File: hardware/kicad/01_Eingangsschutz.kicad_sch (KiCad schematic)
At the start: 4 parts, among them K101 G6S-2F DC5 - C16707, Q111 DMN2056U-7

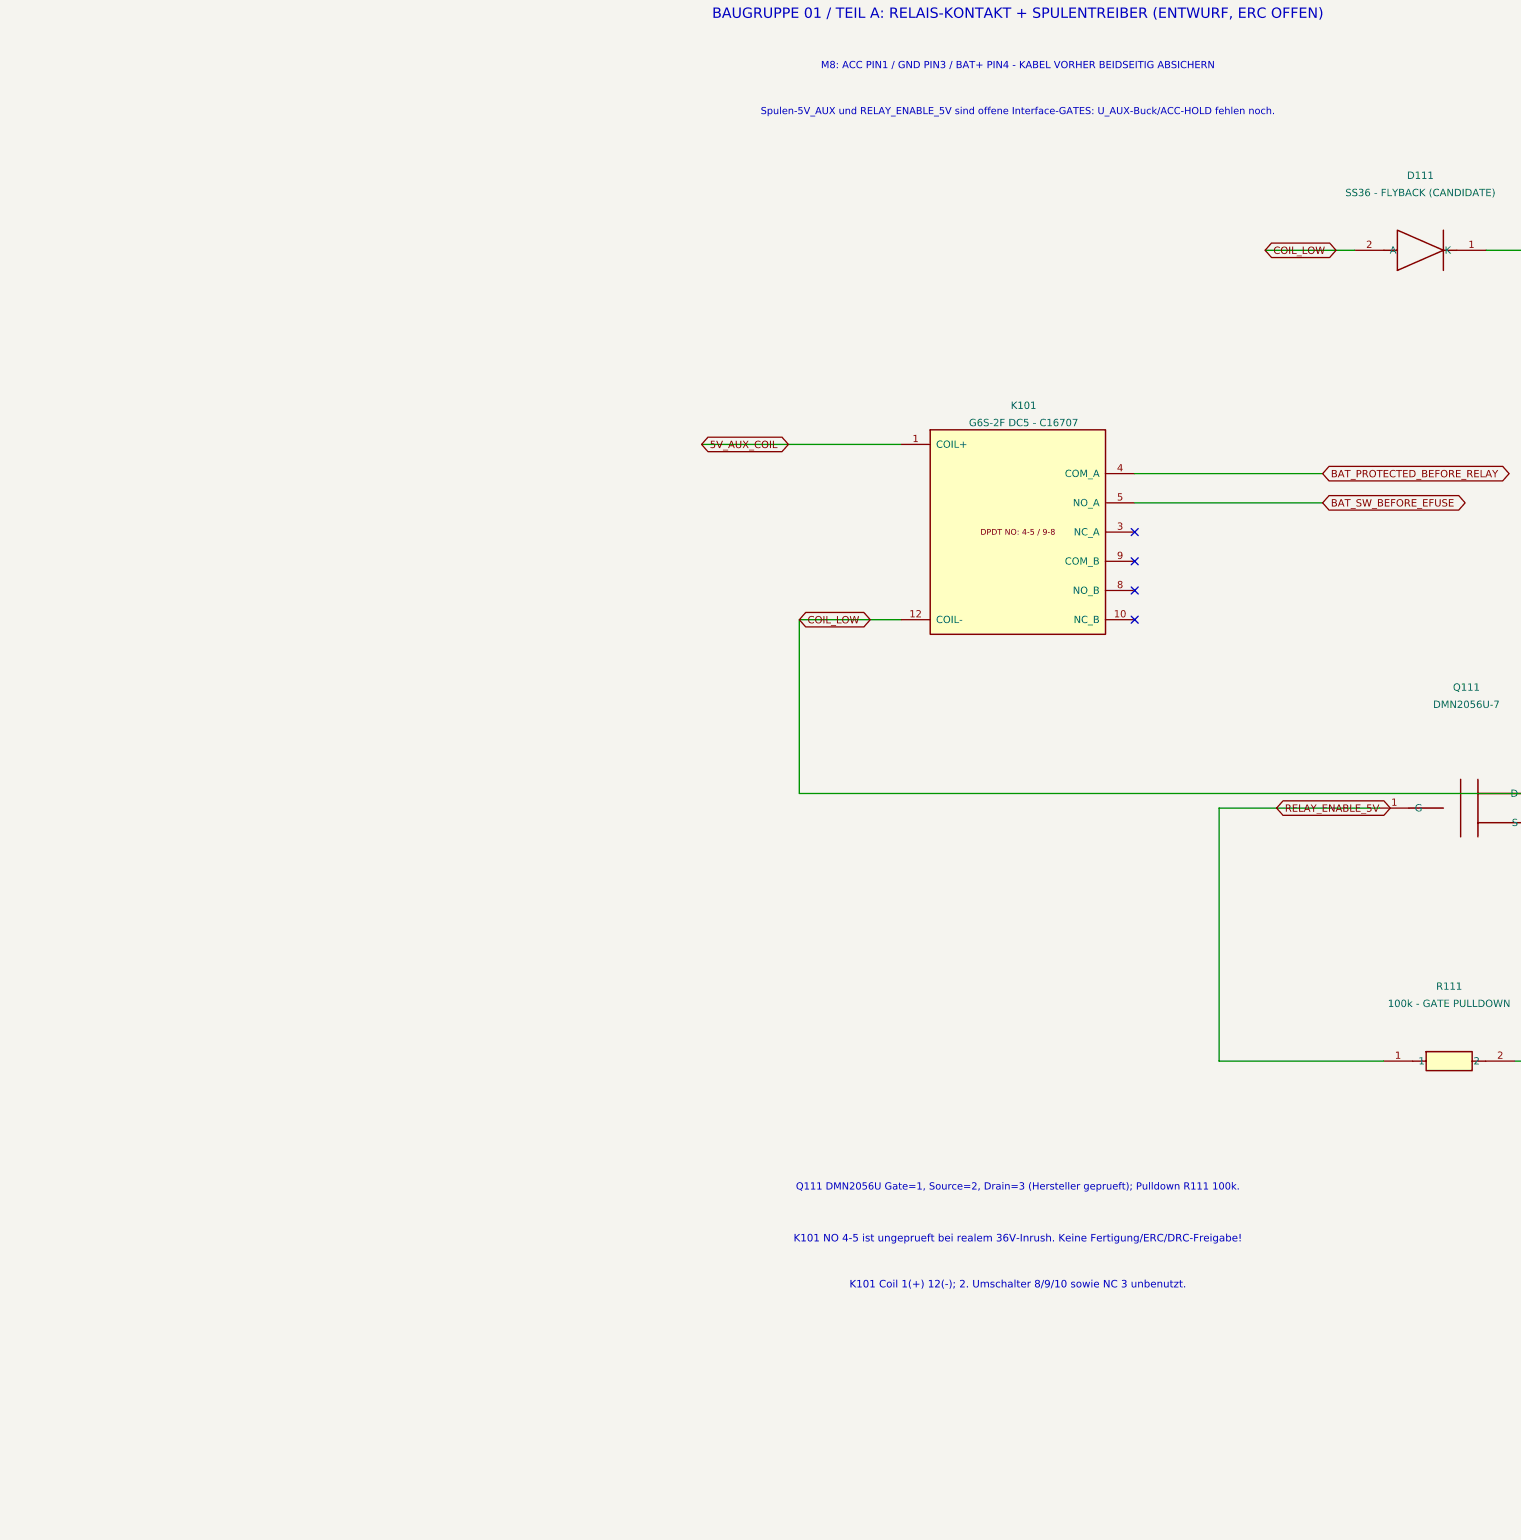
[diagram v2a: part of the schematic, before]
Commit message: hardware(kicad): integrate preliminary LM5164-Q1 5V AUX buck as hierarchical sheet 01A
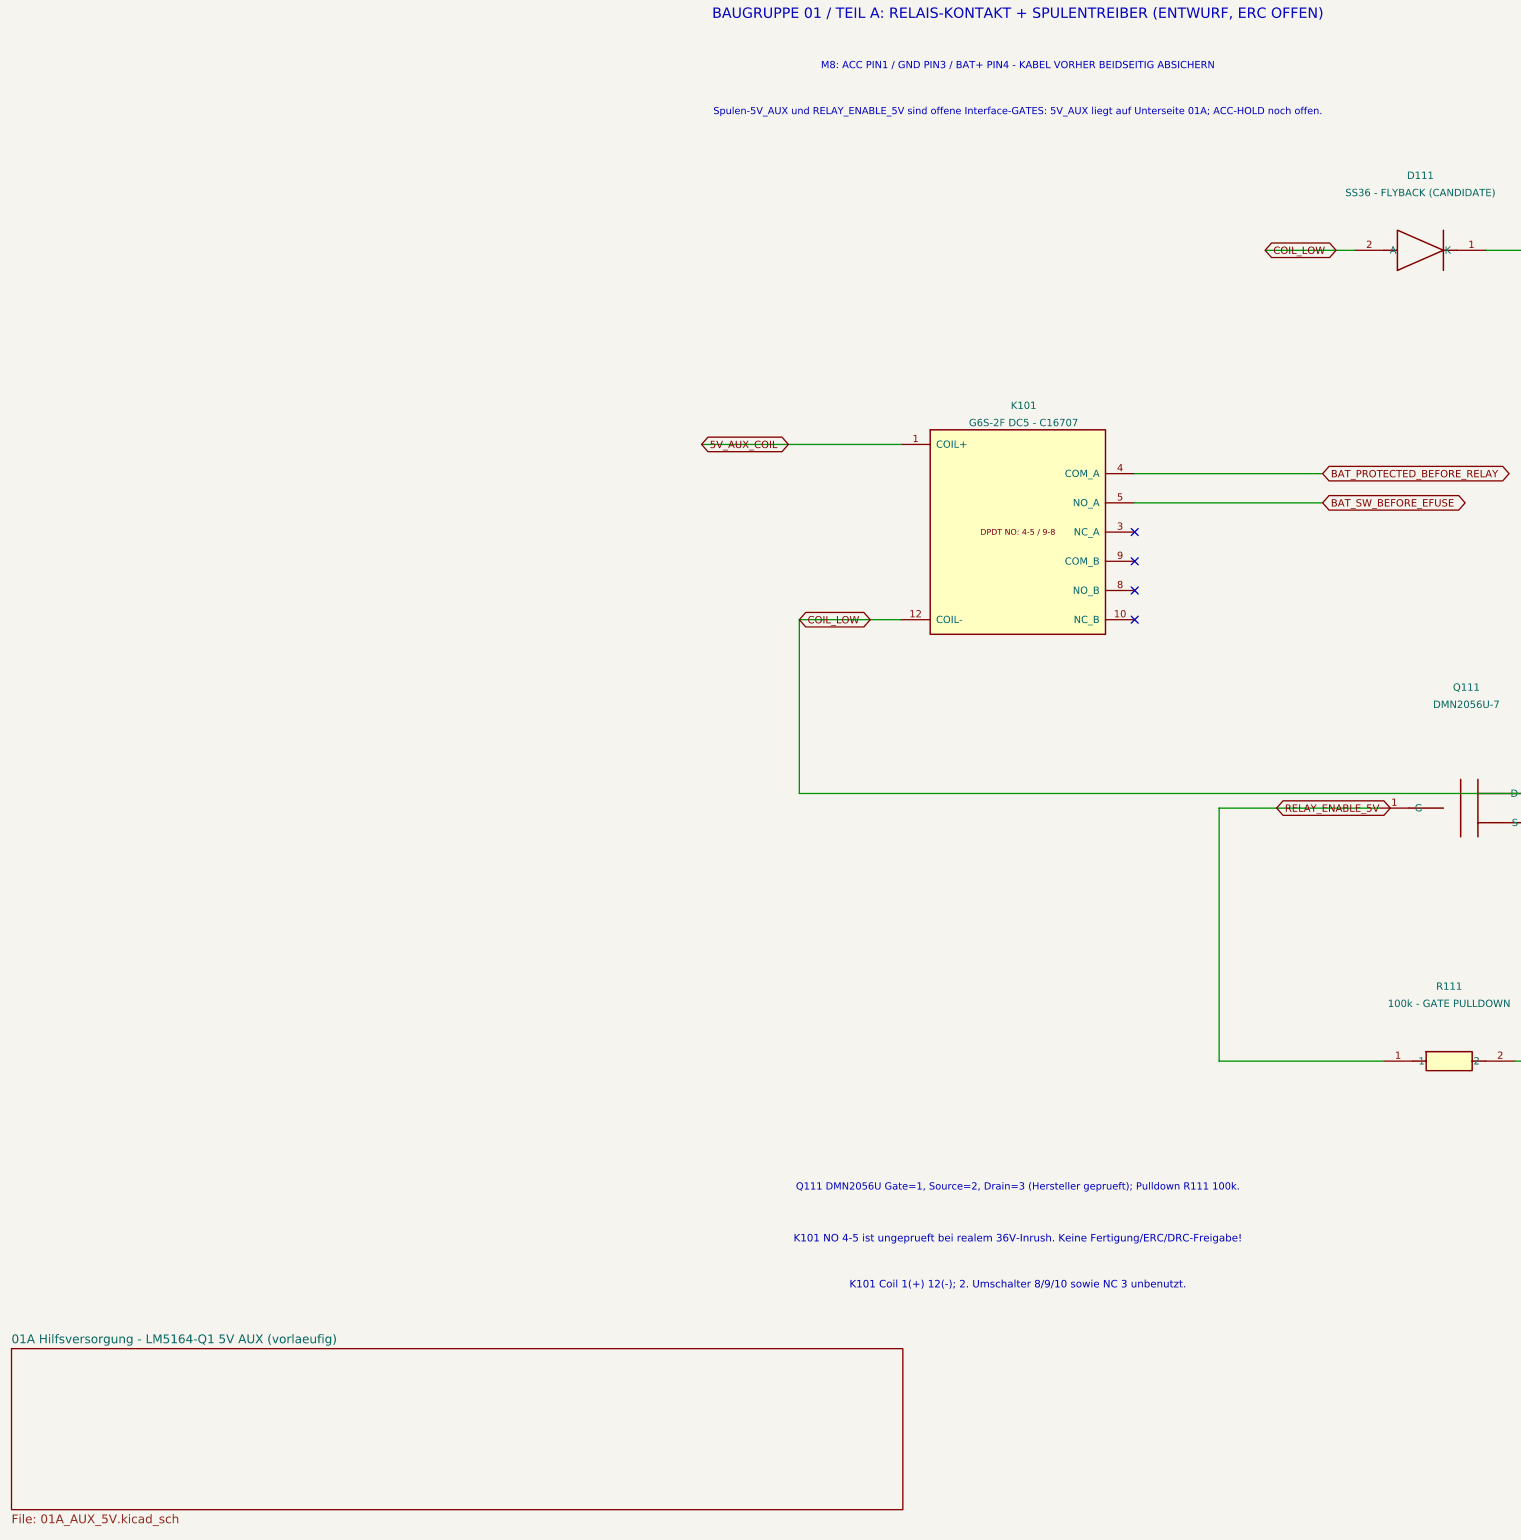
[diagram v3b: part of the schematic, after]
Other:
- added sheet 01A Hilfsversorgung - LM5164-Q1 5V AUX (vorlaeufig) (01A_AUX_5V.kicad_sch)
- note added: "Spulen-5V_AUX und RELAY_ENABLE_5V sind offene Interface-GATES: 5V_AUX liegt auf Unterseite 01A; ACC-HOLD noch offen."
- note removed: "Spulen-5V_AUX und RELAY_ENABLE_5V sind offene Interface-GATES: U_AUX-Buck/ACC-HOLD fehlen noch."
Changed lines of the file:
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@@
 (text "BAUGRUPPE 01 / TEIL A: RELAIS-KONTAKT + SPULENTREIBER (ENTWURF, ERC OFFEN)" (at 200 25 0) (effects (font (size 1.8 1.8))))
 (text "M8: ACC PIN1 / GND PIN3 / BAT+ PIN4 - KABEL VORHER BEIDSEITIG ABSICHERN" (at 200 34 0) (effects (font (size 1.25 1.25))))
-(text "Spulen-5V_AUX und RELAY_ENABLE_5V sind offene Interface-GATES: U_AUX-Buck/ACC-HOLD fehlen noch." (at 200 42 0) (effects (font (size 1.23 1.23))))
+(text "Spulen-5V_AUX und RELAY_ENABLE_5V sind offene Interface-GATES: 5V_AUX liegt auf Unterseite 01A; ACC-HOLD noch offen." (at 200 42 0) (effects (font (size 1.23 1.23))))
 (text "Q111 DMN2056U Gate=1, Source=2, Drain=3 (Hersteller geprueft); Pulldown R111 100k." (at 200 229 0) (effects (font (size 1.25 1.25))))
 (text "K101 NO 4-5 ist ungeprueft bei realem 36V-Inrush. Keine Fertigung/ERC/DRC-Freigabe!" (at 200 238 0) (effects (font (size 1.3 1.3))))
 (text "K101 Coil 1(+) 12(-); 2. Umschalter 8/9/10 sowie NC 3 unbenutzt." (at 200 246 0) (effects (font (size 1.3 1.3))))
+ (sheet (at 25 257) (size 155 28) (exclude_from_sim no) (in_bom yes) (on_board yes) (dnp no)
+ (stroke (width 0) (type solid)) (fill (color 0 0 0 0))
+ (property "Sheetname" "01A Hilfsversorgung - LM5164-Q1 5V AUX (vorlaeufig)" (at 25 256.24 0) (effects (font (size 1.524 1.524)) (justify left bottom)))
+ (property "Sheetfile" "01A_AUX_5V.kicad_sch" (at 25 285.76 0) (effects (font (size 1.524 1.524)) (justify left top)))
+ (instances (project "TripTracer_V1" (path "/a26d9b0c-7f10-4e5a-a65f-000000000064/a26d9b0c-7f10-4e5a-a65f-000000000065" (page "2.1"))))
+)
  (sheet_instances (path "/" (page "2")))
  (embedded_fonts no)

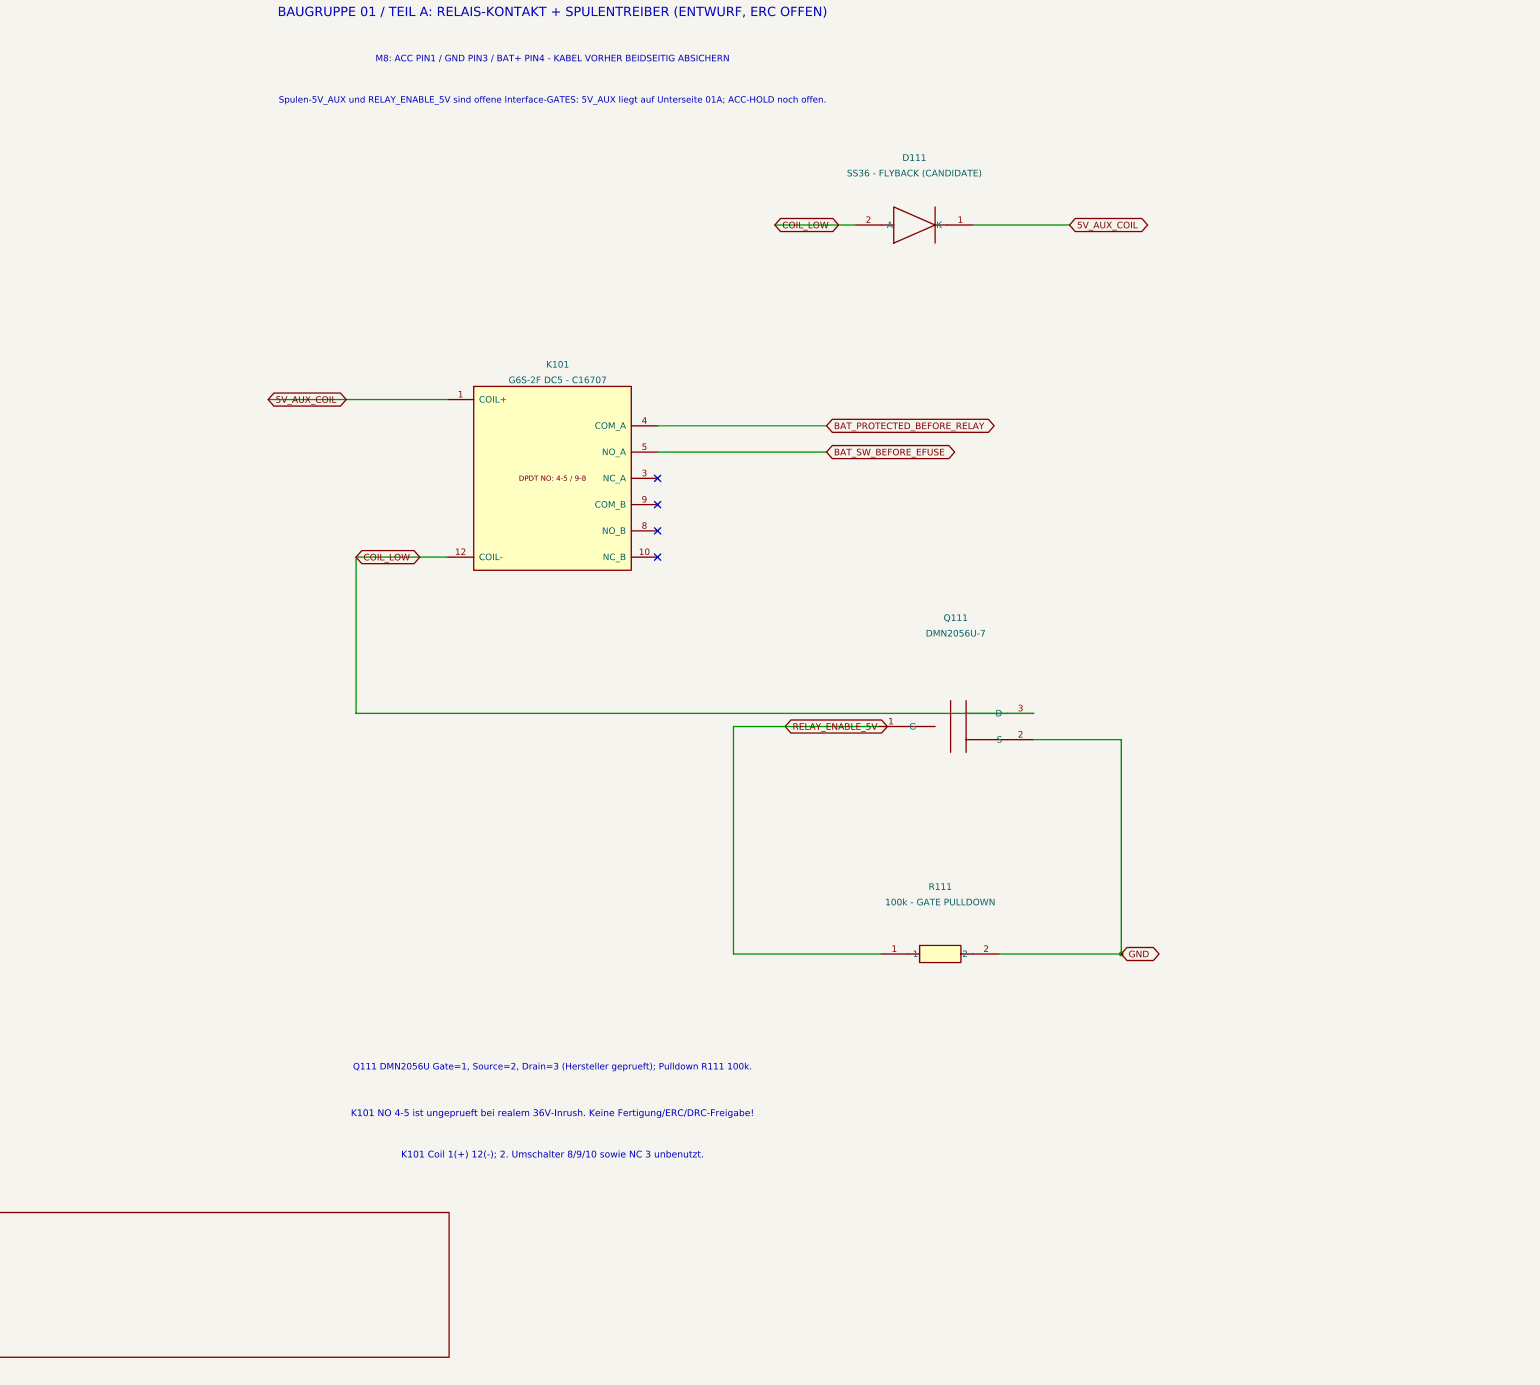
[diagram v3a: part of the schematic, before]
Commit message: hardware(kicad): implement low-quiescent ACC transistor start and isolated HOLD input as sheet 01B
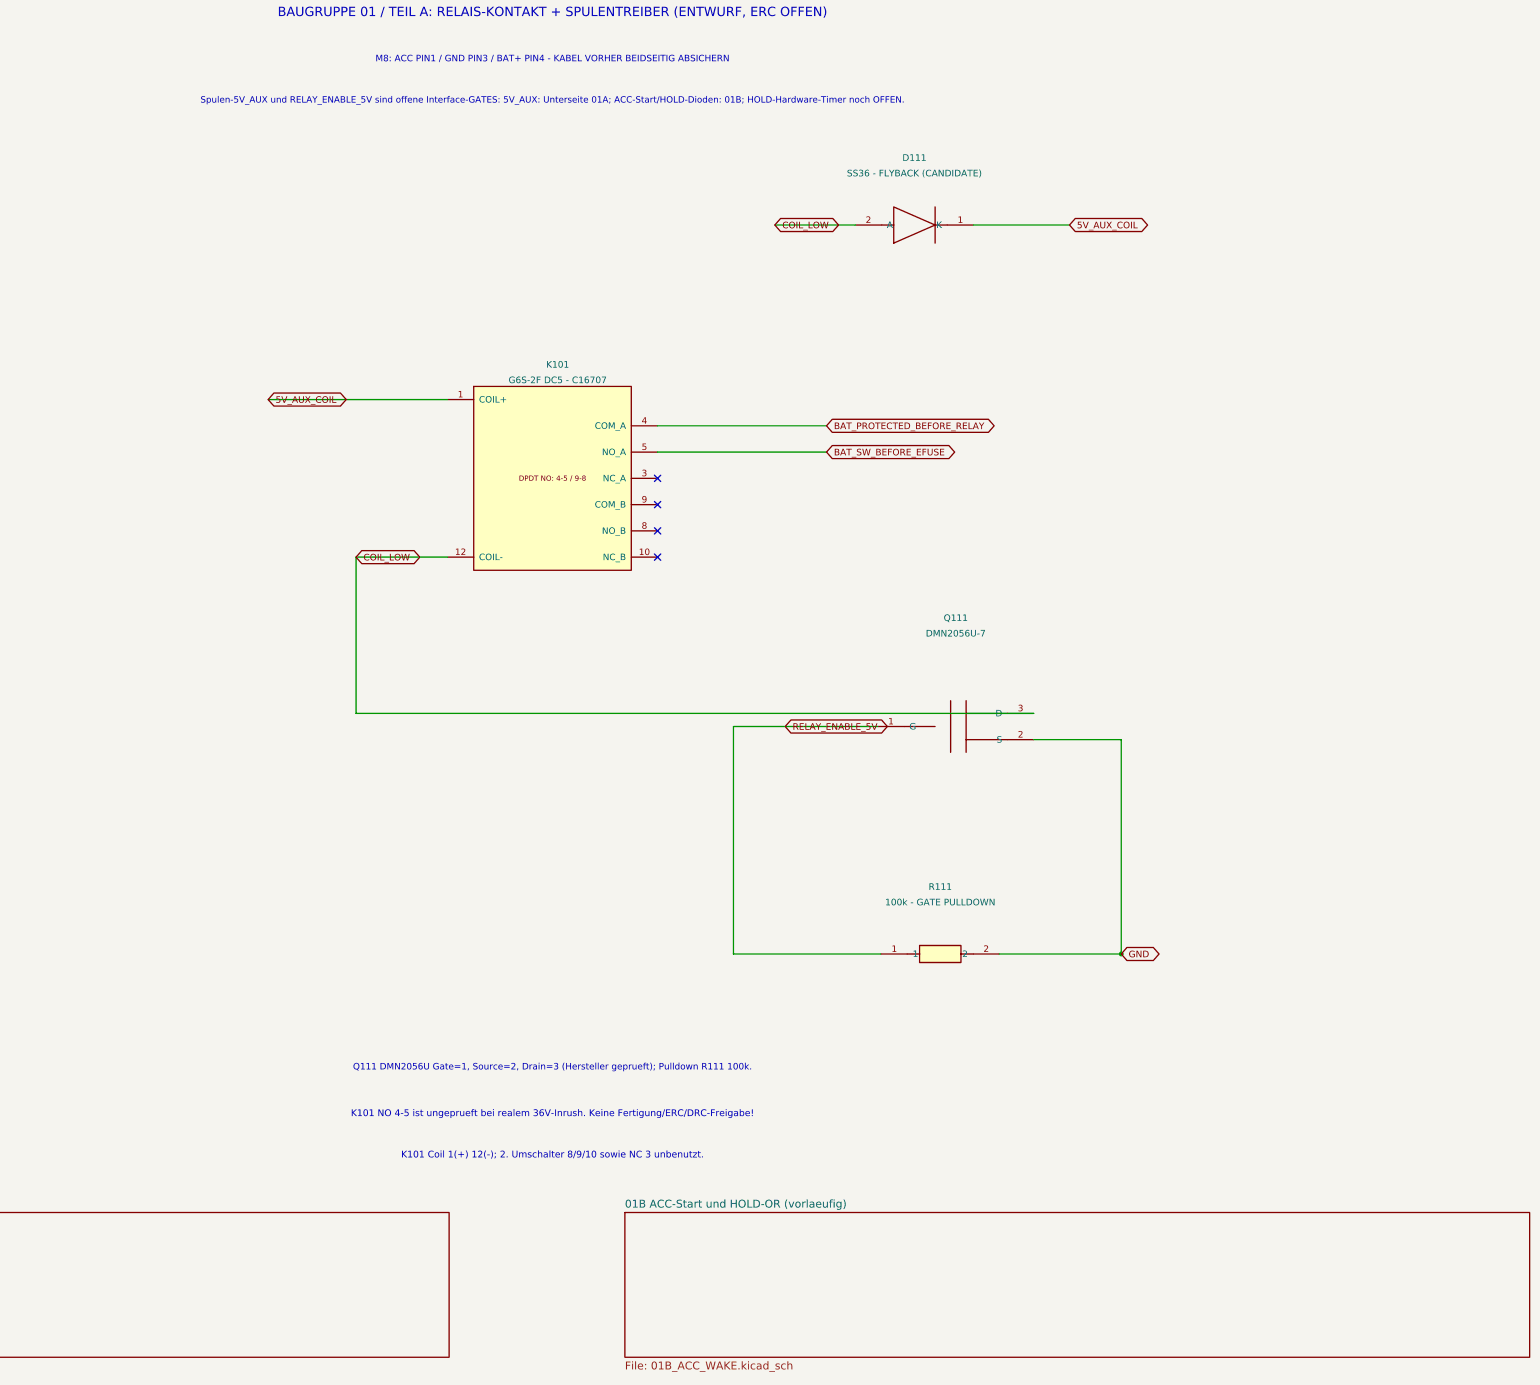
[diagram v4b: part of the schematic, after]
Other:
- added sheet 01B ACC-Start und HOLD-OR (vorlaeufig) (01B_ACC_WAKE.kicad_sch)
- note added: "Spulen-5V_AUX und RELAY_ENABLE_5V sind offene Interface-GATES: 5V_AUX: Unterseite 01A; ACC-Start/HOLD-Dioden: 01B; HOLD-Hardware-Timer noch OFFEN."
- note removed: "Spulen-5V_AUX und RELAY_ENABLE_5V sind offene Interface-GATES: 5V_AUX liegt auf Unterseite 01A; ACC-HOLD noch offen."
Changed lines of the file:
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@@
 (text "BAUGRUPPE 01 / TEIL A: RELAIS-KONTAKT + SPULENTREIBER (ENTWURF, ERC OFFEN)" (at 200 25 0) (effects (font (size 1.8 1.8))))
 (text "M8: ACC PIN1 / GND PIN3 / BAT+ PIN4 - KABEL VORHER BEIDSEITIG ABSICHERN" (at 200 34 0) (effects (font (size 1.25 1.25))))
-(text "Spulen-5V_AUX und RELAY_ENABLE_5V sind offene Interface-GATES: 5V_AUX liegt auf Unterseite 01A; ACC-HOLD noch offen." (at 200 42 0) (effects (font (size 1.23 1.23))))
+(text "Spulen-5V_AUX und RELAY_ENABLE_5V sind offene Interface-GATES: 5V_AUX: Unterseite 01A; ACC-Start/HOLD-Dioden: 01B; HOLD-Hardware-Timer noch OFFEN." (at 200 42 0) (effects (font (size 1.23 1.23))))
 (text "Q111 DMN2056U Gate=1, Source=2, Drain=3 (Hersteller geprueft); Pulldown R111 100k." (at 200 229 0) (effects (font (size 1.25 1.25))))
 (text "K101 NO 4-5 ist ungeprueft bei realem 36V-Inrush. Keine Fertigung/ERC/DRC-Freigabe!" (at 200 238 0) (effects (font (size 1.3 1.3))))
@@
  (instances (project "TripTracer_V1" (path "/a26d9b0c-7f10-4e5a-a65f-000000000064/a26d9b0c-7f10-4e5a-a65f-000000000065" (page "2.1"))))
 )
+ (sheet (at 214 257) (size 175 28) (exclude_from_sim no) (in_bom yes) (on_board yes) (dnp no)
+ (stroke (width 0) (type solid)) (fill (color 0 0 0 0))
+ (property "Sheetname" "01B ACC-Start und HOLD-OR (vorlaeufig)" (at 214 256.24 0) (effects (font (size 1.524 1.524)) (justify left bottom)))
+ (property "Sheetfile" "01B_ACC_WAKE.kicad_sch" (at 214 285.76 0) (effects (font (size 1.524 1.524)) (justify left top)))
+ (instances (project "TripTracer_V1" (path "/a26d9b0c-7f10-4e5a-a65f-000000000064/a26d9b0c-7f10-4e5a-a65f-000000000065" (page "2.2"))))
+)
  (sheet_instances (path "/" (page "2")))
